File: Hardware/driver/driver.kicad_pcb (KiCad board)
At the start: 4 copper layers, 128.1 x 184.5 mm, 176 parts, among them J201 Conn_02x10_Odd_Even, J302 Würth 74651194R, J303 Würth 74651194R, J401 TBP02R2W-381-03BE, J402 Conn_01x02_Male, J501 Conn_Coaxial, J601 Screw_Terminal_01x02, K601 EC2-5TNU, M201 Fan_4pin, Q201 MMBT3904, Q202 PN2222A, Q301 IXTH80N075L2, Q302 IXTH80N075L2, Q601 MMBT3904, Q602 MMBT3904, U101 ICL7660, U102 DS2482-100, U103 PI4IOE5V9536, U201 AT24CS32-SSHM, U202 NCP716BCSN330T1G, U203 ADUM1250, U205 FODM217B, U206 EMC2101-R, U207 MCP1703AT-5002E/DB, U301 MCP3421A2T-ECH, U302 OPA2388, U303 DAC60501Z, U304 LM431SC, U305 MCP3421A3T-ECH, U306 OPA2388, U307 DAC60501Z, U308 LM431SC, U309 DS18B20, U310 DS18B20, U501 74LVC1G17, U502 FODM217B, U601 MCP3421A1T-ECH, U602 OPA277

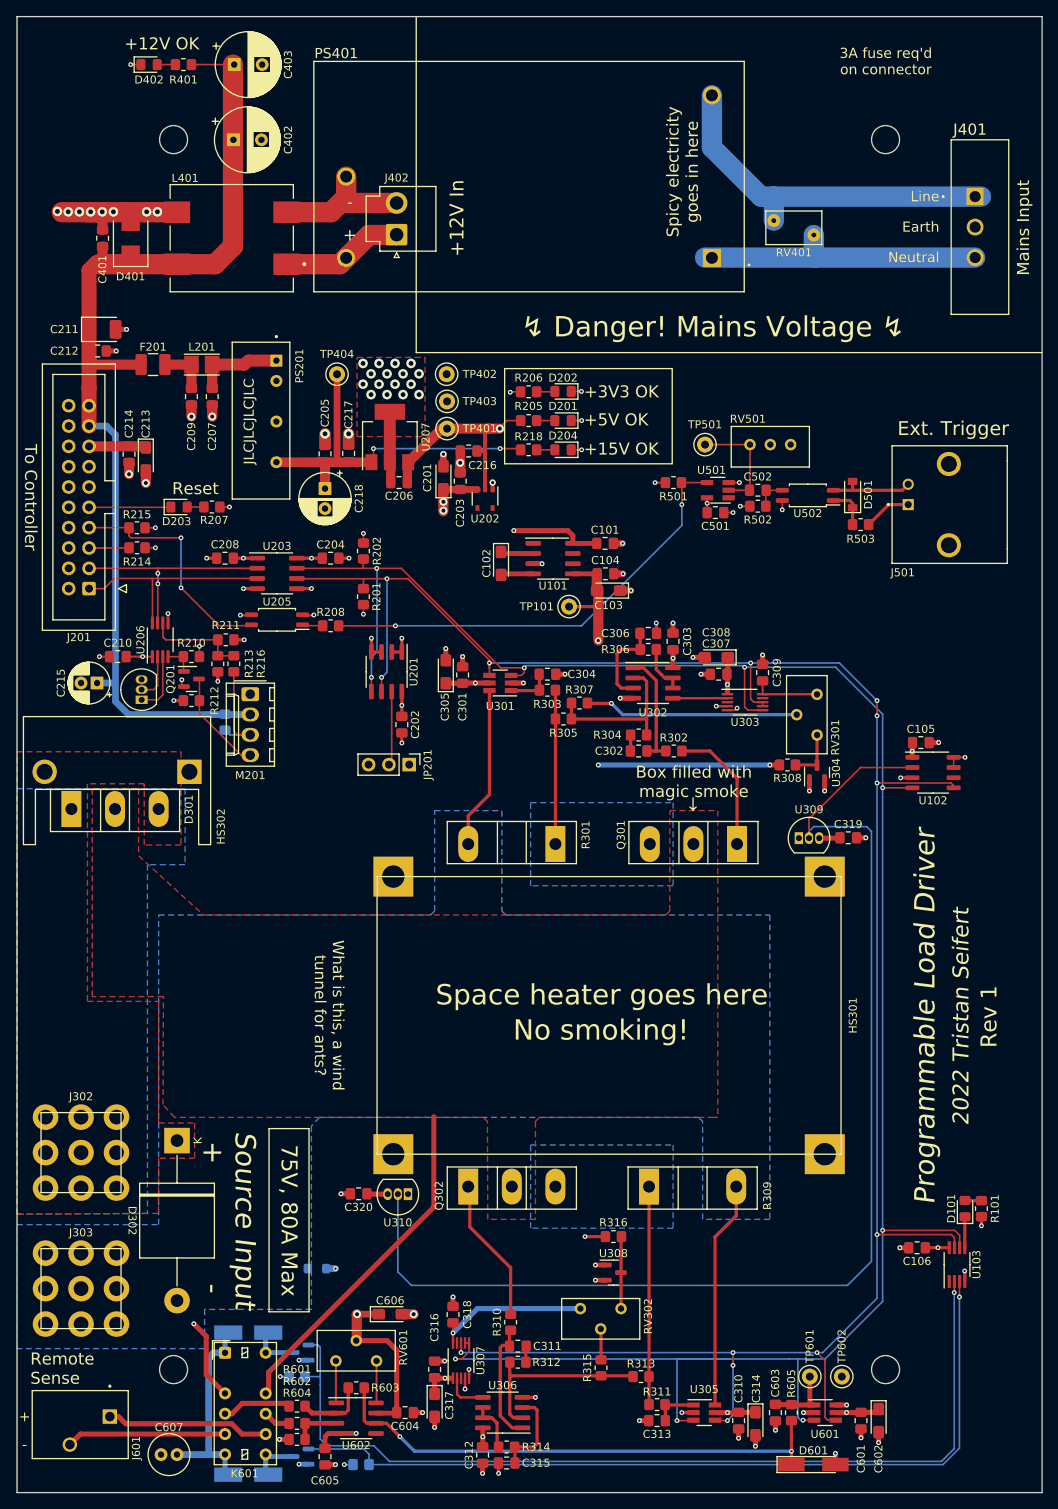
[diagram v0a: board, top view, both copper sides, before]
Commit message: More rev 2 driver board work
- Updated power supply section with linear regulators for the +12V and
  +5V rails

- Replaced op amps for driving the MOSFETs with different ones, and
  updated them so that they actually run off the 12V rail instead of the
  3V3 rail.
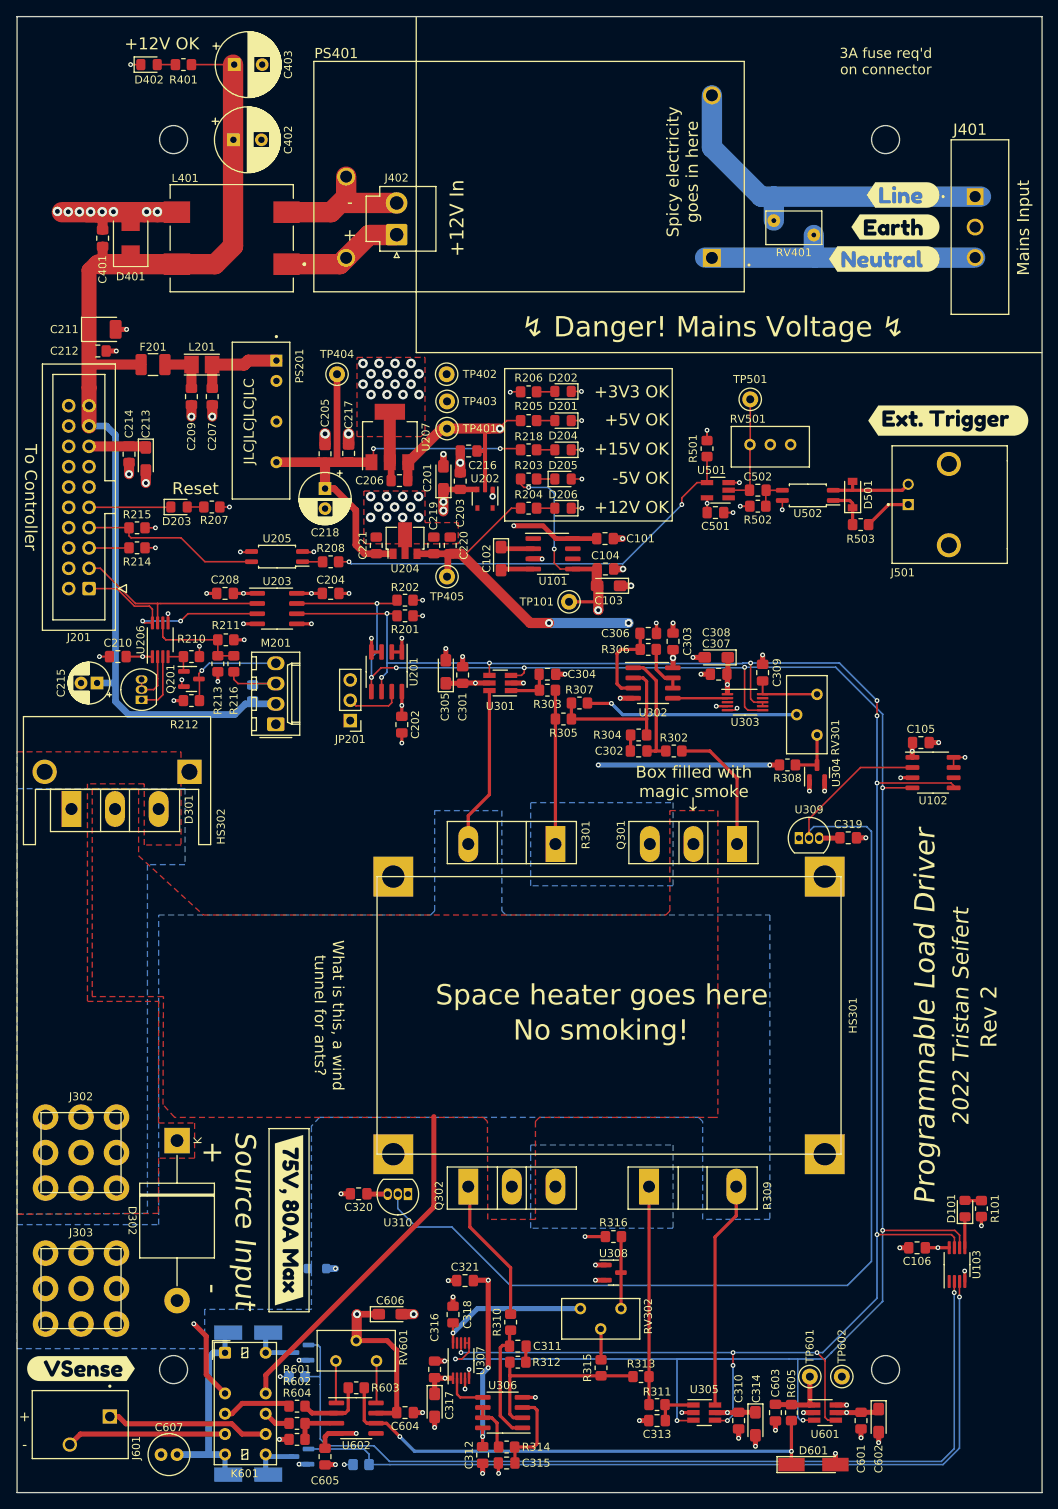
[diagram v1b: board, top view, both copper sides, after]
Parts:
- added C219: 100nF, Capacitor_SMD:C_0805_2012Metric_Pad1.18x1.45mm_HandSolder, F.Cu at (72.1, 86.1)
- added C220: 4.7µF, Capacitor_SMD:C_0805_2012Metric_Pad1.18x1.45mm_HandSolder, F.Cu at (74.2, 86.1)
- added C221: 4.7µF, Capacitor_SMD:C_0805_2012Metric_Pad1.18x1.45mm_HandSolder, F.Cu at (64.9, 86.1)
- added C321: 1µF, Capacitor_SMD:C_0805_2012Metric_Pad1.18x1.45mm_HandSolder, F.Cu at (76.0, 178.0)
- added D205: Green, LED_SMD:LED_0805_2012Metric_Pad1.15x1.40mm_HandSolder, F.Cu at (88.2, 77.8)
- added D206: Green, LED_SMD:LED_0805_2012Metric_Pad1.15x1.40mm_HandSolder, F.Cu at (88.2, 81.5)
- added R203: 2k2, Resistor_SMD:R_0805_2012Metric_Pad1.20x1.40mm_HandSolder, F.Cu at (84.0, 77.8)
- added R204: 4k99, Resistor_SMD:R_0805_2012Metric_Pad1.20x1.40mm_HandSolder, F.Cu at (84.0, 81.5)
- added TP405: +12V, TestPoint:TestPoint_Keystone_5000-5004_Miniature, F.Cu at (73.8, 90.0)
- added U204: MCP1804x-C002xMB, Package_TO_SOT_SMD:SOT-89-3, F.Cu at (68.5, 85.5)
- added kibuzzard-6248DD82: G***, kibuzzard-6248DD82, F.Cu at (136.4, 70.5)
- added kibuzzard-6248DDB7: G***, kibuzzard-6248DDB7, F.Cu at (130.8, 42.3)
- added kibuzzard-6248DE02: G***, kibuzzard-6248DE02, F.Cu at (129.8, 46.3)
- added kibuzzard-6248DE32: G***, kibuzzard-6248DE32, F.Cu at (128.4, 50.3)
- added kibuzzard-6248DECB: G***, kibuzzard-6248DECB, F.Cu at (54.0, 170.4)
- added kibuzzard-6248DF28: G***, kibuzzard-6248DF28, F.Cu at (28.0, 189.0)
- U302, U306: value OPA2388 -> ADA4522-2
- moved JP201 9.20 mm to (61.6, 108.0), turned to 180 degrees
- moved R202 8.05 mm to (68.5, 93.0), turned to 0 degrees
- moved R208 8.00 mm to (59.2, 88.2)
- moved TP501 8.00 mm to (111.7, 67.8)
- moved U205 7.90 mm to (52.5, 87.5)
- moved R501 5.98 mm to (106.2, 74.0), turned to -90 degrees
- moved R201 5.73 mm to (68.5, 94.9), turned to 0 degrees
- moved R217 5.02 mm to (49.5, 104.5), turned to -90 degrees
- moved M201 4.93 mm to (52.4, 108.5), turned to 90 degrees
- moved U203 4.40 mm to (52.5, 94.0)
- moved C204 4.40 mm to (59.2, 92.1)
- moved C208 4.40 mm to (46.0, 92.1)
- moved C104 0.60 mm to (93.5, 89.0)
- moved C101 0.60 mm to (93.5, 85.2)
- moved C102 0.60 mm to (80.5, 87.8)
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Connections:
- C303 pad 1: +3V3 -> +12V
- C312 pad 1: +3V3 -> +12V
- U302 pad 8: +3V3 -> +12V
- U306 pad 8: +3V3 -> +12V
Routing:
- net +12V: track 0.00 -> 172.4 mm, vias 0 -> 6
- net -5V: track 165.1 -> 182.4 mm, vias 5 -> 7
- net +15V: track 46.4 -> 60.8 mm
- net /I2C_SDA: track 275.8 -> 266.2 mm
- net /I2C_SCL: track 282.5 -> 274.8 mm, vias 9 -> 10
- net /External Interface/~{EXT_TRIG}: track 29.6 -> 22.7 mm, vias 2 -> 0
- net /1WIRE: track 151.7 -> 147.1 mm
- net +3V3: track 63.4 -> 59.1 mm, vias 21 -> 19
- net +12VA: track 133.5 -> 137.3 mm
- net Net-(M201-Pad3): track 13.1 -> 9.39 mm
- net GNDA: track 40.0 -> 43.4 mm
- net GND: track 107.6 -> 110.9 mm, vias 86 -> 100
- net /TRIGGER: track 57.1 -> 54.1 mm
- net /External Interface/EXT_SDA: track 27.9 -> 25.3 mm, vias 2 -> 0
- net Net-(JP201-Pad2): track 9.27 -> 6.96 mm
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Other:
- board text added: "-5V OK"
- board text added: "Rev 2"
- board text removed: "75V, 80A Max"
- board text removed: "Earth"
- board text removed: "Ext. Trigger"
- board text removed: "Line"
- board text removed: "Neutral"
- board text removed: "Remote Sense"
- board text removed: "Rev 1"

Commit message: Case boss cutouts on driver board
- Added cutouts on the front edges of the load board to make space for
  the bosses that hold the case's screw mounts.
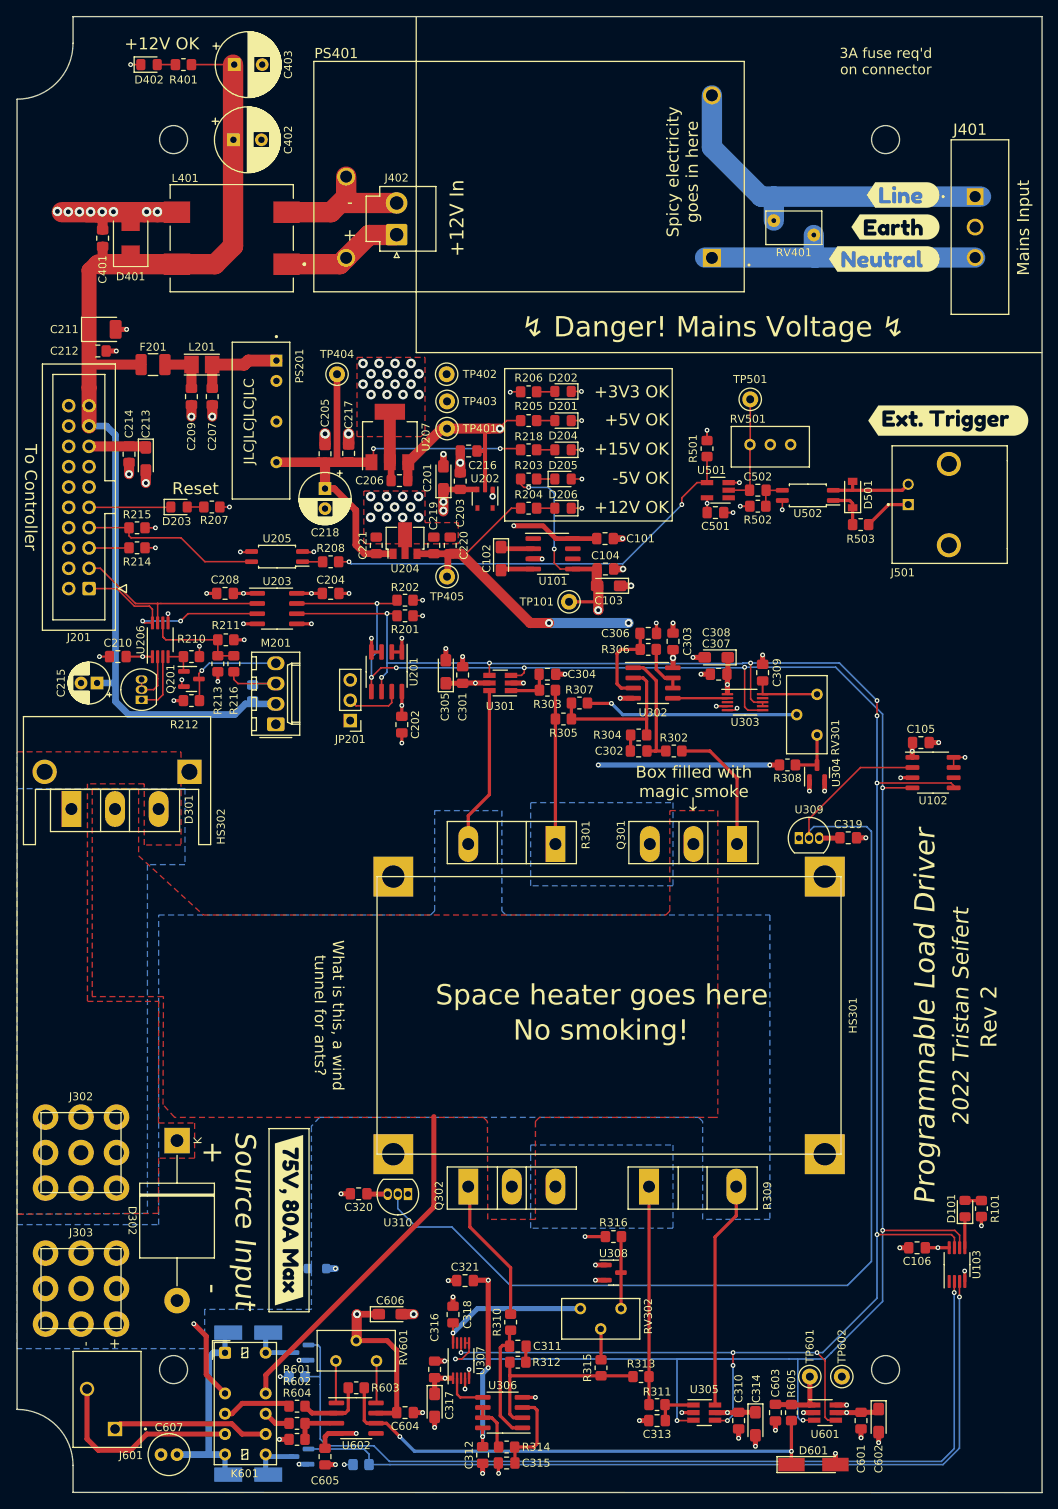
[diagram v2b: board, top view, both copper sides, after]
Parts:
- removed kibuzzard-6248DF28: G***, kibuzzard-6248DF28
- moved J601 1.68 mm to (32.2, 196.6), turned to 180 degrees
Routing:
- net /Input Stage/Voltage Sense/SENSE-: track 19.9 -> 24.9 mm
- net /Input Stage/Voltage Sense/SENSE+: track 20.4 -> 19.6 mm
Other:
- outline, holes or cut-outs redrawn

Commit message: More work on rev2 driver board
- Tweaked the board layout for the load driver some more, primarily
  relating to power and friends

- Fixed footprint of fan connector on driver board (to properly have the
  mechanical mounting hole)

- Manufacturability/solderability tweaks for a few other footprints
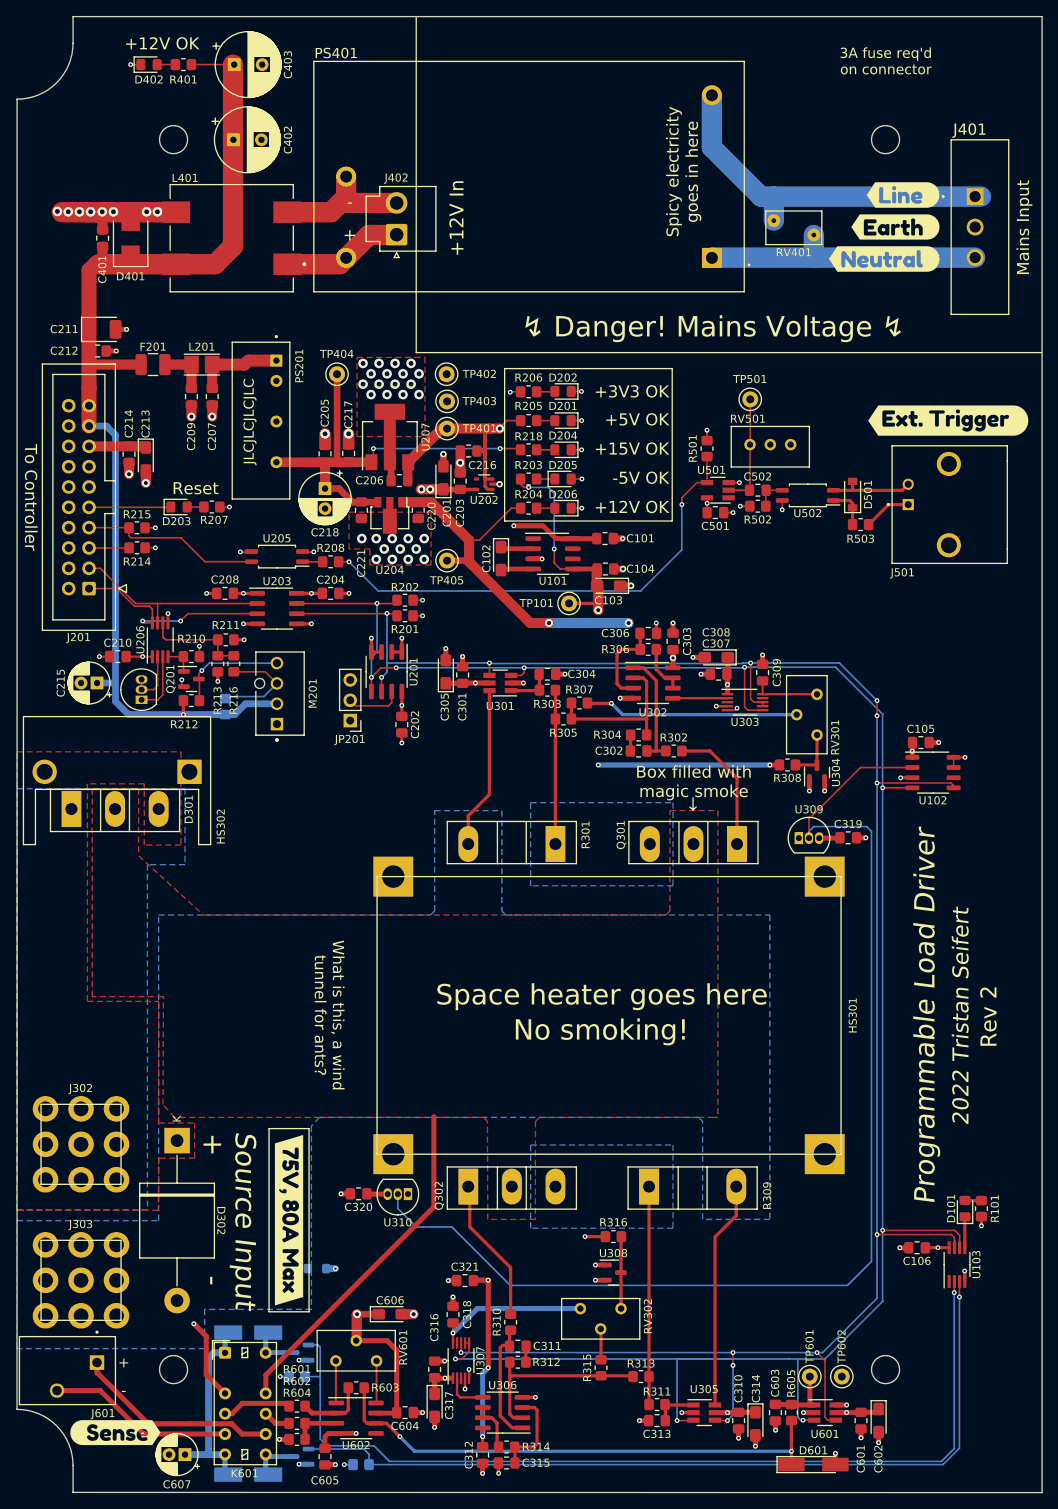
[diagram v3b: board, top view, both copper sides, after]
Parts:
- removed C219: 100nF, Capacitor_SMD:C_0805_2012Metric_Pad1.18x1.45mm_HandSolder
- added kibuzzard-6250772E: G***, kibuzzard-6250772E, F.Cu at (32.3, 197.0)
- C607: footprint Capacitor_THT:C_Radial_D5.0mm_H11.0mm_P2.00mm -> Capacitor_THT:CP_Radial_D5.0mm_P2.00mm
- M201: footprint Connector_Molex:Molex_KK-254_AE-6410-04A_1x04_P2.54mm_Vertical -> programmable-load:Molex-47053-1000-MFG
- U202: value NCP716BCSN330T1G -> MIC5366-3.3YC5; footprint Package_SO:TSOP-5_1.65x3.05mm_P0.95mm -> Package_TO_SOT_SMD:SOT-353_SC-70-5
- moved J601 8.60 mm to (30.0, 188.2), turned to -90 degrees
- moved C220 5.95 mm to (70.2, 81.7), turned to -90 degrees
- moved C221 4.77 mm to (63.0, 81.7), turned to -90 degrees
- moved M201 3.86 mm to (52.9, 104.6), turned to -90 degrees
- moved R217 3.80 mm to (46.0, 106.2)
- moved U204 3.68 mm to (66.6, 82.3), turned to -90 degrees
- moved TP405 2.00 mm to (73.8, 88.0)
- moved U202 1.82 mm to (78.4, 78.5), turned to 180 degrees
- moved J302 1.03 mm to (28.0, 161.0)
- moved J303 1.03 mm to (28.0, 178.0)
- moved C607 1.00 mm to (41.0, 199.8)
- moved TP101 0.20 mm to (89.0, 93.3)
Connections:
- R212 pad 2: +3V3A -> +12VA
- U202 pad 1: GND -> +5V
- U202 pad 2: +5V -> GND
- U202 pad 3: +3V3 -> +5V
- U202 pad 5: unconnected-(U202-Pad5) -> +3V3
- U204 pad 1: +15V -> +12V
- U204 pad 3: +12V -> +15V
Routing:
- net +15V: track 60.8 -> 53.7 mm
- net /TRIGGER: track 54.1 -> 60.2 mm
- net /Input Stage/Voltage Sense/SENSE+: track 19.6 -> 25.5 mm
- net Net-(M201-Pad3): track 9.39 -> 13.2 mm
- net +12V: track 172.4 -> 175.2 mm
- net +12VA: track 137.3 -> 139.2 mm, vias 0 -> 1
- net /Input Stage/Voltage Sense/SENSE-: track 24.9 -> 23.3 mm
- net +3V3A: track 21.0 -> 19.8 mm, vias 8 -> 7
- net /Mains Supply (Optional)/MAINS_N: track 36.6 -> 35.8 mm
- net GND: vias 100 -> 101
